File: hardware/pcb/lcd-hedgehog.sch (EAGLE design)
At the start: 40 parts

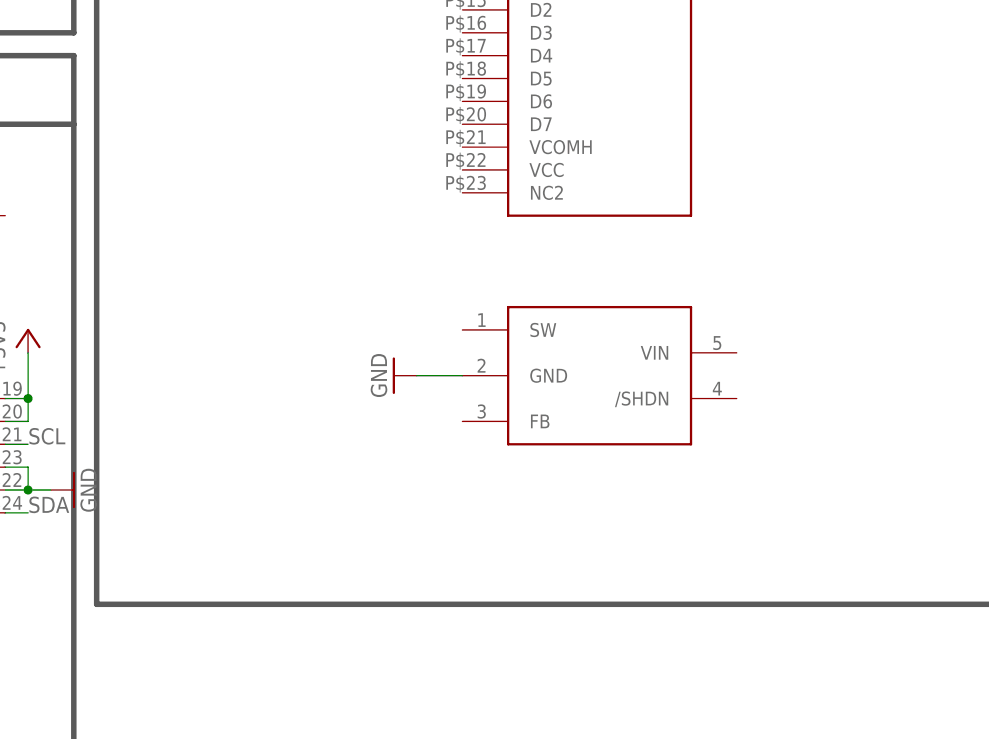
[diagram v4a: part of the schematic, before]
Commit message: added 12V power circuit2
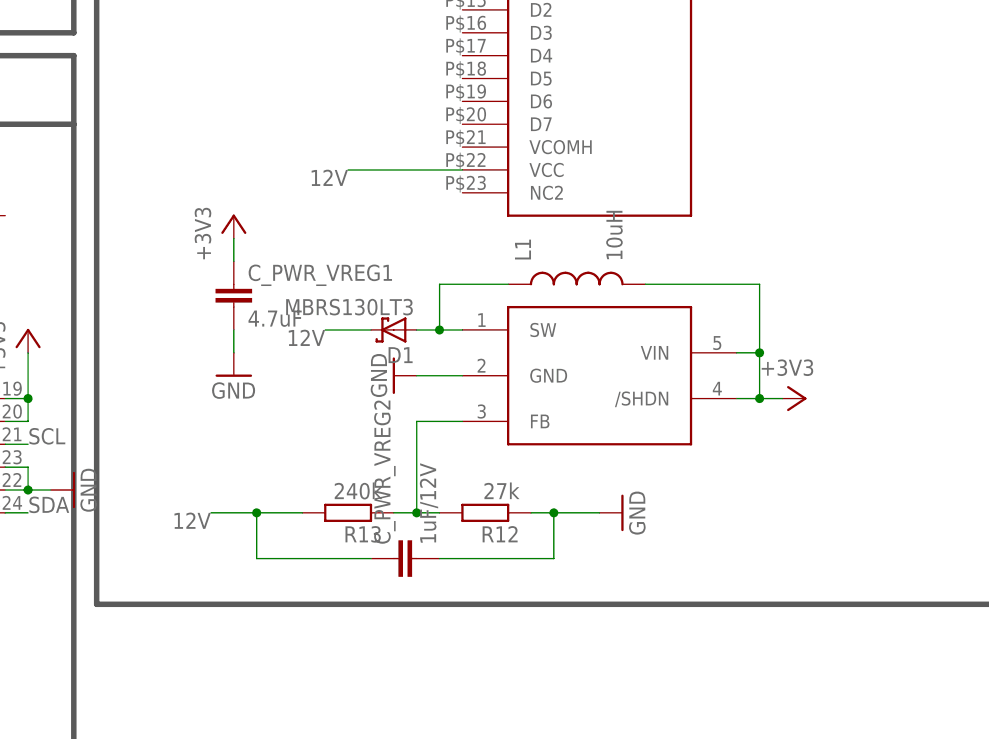
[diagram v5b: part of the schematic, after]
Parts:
- added C_PWR_VREG1: 4.7uF, rcl:C-EUC0603K
- added C_PWR_VREG2: 1uF/12V, rcl:C-EUC0603K
- added D1: MBRS130LT3, diode:MBRS130LT3
- added L1: 10uH, jnode:SPARKFUN_INDUCTOR0603
- added R12: 27k, rcl:R-EU_R0603
- added R13: 240k, rcl:R-EU_R0603
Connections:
- new net 12V: C_PWR_VREG2.1, D1.C, R13.2, U$4.VCC
- new net N$15: R12.2, R13.1, U$5.FB
- new net N$16: D1.A, L1.1, U$5.SW
- net +3V3: now also C_PWR_VREG1.1, L1.2, U$5./SHDN, U$5.VIN
- net GND: now also C_PWR_VREG1.2, C_PWR_VREG2.2, R12.1
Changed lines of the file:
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@@
 <part name="GND32" library="supply1" deviceset="GND" device=""/>
 <part name="C66" library="rcl" deviceset="C-EU" device="C0805K" value="10uF"/>
+<part name="C_PWR_VREG1" library="rcl" deviceset="C-EU" device="C0603K" value="4.7uF"/>
+<part name="R12" library="rcl" deviceset="R-EU_" device="R0603" value="27k"/>
+<part name="R13" library="rcl" deviceset="R-EU_" device="R0603" value="240k"/>
+<part name="GND33" library="supply1" deviceset="GND" device=""/>
+<part name="C_PWR_VREG2" library="rcl" deviceset="C-EU" device="C0603K" value="1uF/12V"/>
+<part name="GND34" library="supply1" deviceset="GND" device=""/>
+<part name="+3V19" library="supply1" deviceset="+3V3" device=""/>
+<part name="+3V20" library="supply1" deviceset="+3V3" device=""/>
+<part name="L1" library="jnode" deviceset="SPARKFUN_INDUCTOR" device="0603" value="10uH"/>
+<part name="D1" library="diode" deviceset="MBRS130LT3" device=""/>
 </parts>
 <sheets>
@@
 <instance part="GND32" gate="1" x="160.02" y="-35.56" rot="R90"/>
 <instance part="C66" gate="G$1" x="149.86" y="-35.56" rot="R90"/>
+<instance part="C_PWR_VREG1" gate="G$1" x="193.04" y="38.1"/>
+<instance part="R12" gate="G$1" x="220.98" y="12.7" rot="R180"/>
+<instance part="R13" gate="G$1" x="205.74" y="12.7" rot="R180"/>
+<instance part="GND33" gate="1" x="236.22" y="12.7" rot="R90"/>
+<instance part="C_PWR_VREG2" gate="G$1" x="210.82" y="7.62" rot="R90"/>
+<instance part="GND34" gate="1" x="193.04" y="27.94"/>
+<instance part="+3V19" gate="G$1" x="193.04" y="45.72"/>
+<instance part="+3V20" gate="G$1" x="256.54" y="25.4" rot="R270"/>
+<instance part="L1" gate="G$1" x="231.14" y="38.1" rot="R90"/>
+<instance part="D1" gate="G$1" x="210.82" y="33.02" rot="R180"/>
 </instances>
 <busses>
@@
 <wire x1="154.94" y1="-35.56" x2="157.48" y2="-35.56" width="0.1524" layer="91"/>
 </segment>
+<segment>
+<pinref part="R12" gate="G$1" pin="1"/>
+<pinref part="GND33" gate="1" pin="GND"/>
+<wire x1="226.06" y1="12.7" x2="228.6" y2="12.7" width="0.1524" layer="91"/>
+<pinref part="C_PWR_VREG2" gate="G$1" pin="2"/>
+<wire x1="228.6" y1="12.7" x2="233.68" y2="12.7" width="0.1524" layer="91"/>
+<wire x1="215.9" y1="7.62" x2="228.6" y2="7.62" width="0.1524" layer="91"/>
+<wire x1="228.6" y1="7.62" x2="228.6" y2="12.7" width="0.1524" layer="91"/>
+<junction x="228.6" y="12.7"/>
+</segment>
+<segment>
+<pinref part="GND34" gate="1" pin="GND"/>
+<pinref part="C_PWR_VREG1" gate="G$1" pin="2"/>
+<wire x1="193.04" y1="33.02" x2="193.04" y2="30.48" width="0.1524" layer="91"/>
+</segment>
 </net>
 <net name="D+" class="0">
@@
 <junction x="144.78" y="-35.56"/>
 <junction x="144.78" y="-15.24"/>
+</segment>
+<segment>
+<pinref part="+3V19" gate="G$1" pin="+3V3"/>
+<pinref part="C_PWR_VREG1" gate="G$1" pin="1"/>
+<wire x1="193.04" y1="40.64" x2="193.04" y2="43.18" width="0.1524" layer="91"/>
+</segment>
+<segment>
+<pinref part="U$5" gate="G$1" pin="/SHDN"/>
+<pinref part="+3V20" gate="G$1" pin="+3V3"/>
+<wire x1="254" y1="25.4" x2="251.46" y2="25.4" width="0.1524" layer="91"/>
+<pinref part="U$5" gate="G$1" pin="VIN"/>
+<wire x1="251.46" y1="25.4" x2="248.92" y2="25.4" width="0.1524" layer="91"/>
+<wire x1="248.92" y1="30.48" x2="251.46" y2="30.48" width="0.1524" layer="91"/>
+<wire x1="251.46" y1="30.48" x2="251.46" y2="25.4" width="0.1524" layer="91"/>
+<junction x="251.46" y="25.4"/>
+<pinref part="L1" gate="G$1" pin="2"/>
+<wire x1="238.76" y1="38.1" x2="251.46" y2="38.1" width="0.1524" layer="91"/>
+<wire x1="251.46" y1="38.1" x2="251.46" y2="30.48" width="0.1524" layer="91"/>
+<junction x="251.46" y="30.48"/>
 </segment>
 </net>
@@
 </segment>
 </net>
+<net name="N$15" class="0">
+<segment>
+<pinref part="R12" gate="G$1" pin="2"/>
+<pinref part="R13" gate="G$1" pin="1"/>
+<wire x1="215.9" y1="12.7" x2="213.36" y2="12.7" width="0.1524" layer="91"/>
+<pinref part="U$5" gate="G$1" pin="FB"/>
+<wire x1="213.36" y1="12.7" x2="210.82" y2="12.7" width="0.1524" layer="91"/>
+<wire x1="218.44" y1="22.86" x2="213.36" y2="22.86" width="0.1524" layer="91"/>
+<wire x1="213.36" y1="22.86" x2="213.36" y2="12.7" width="0.1524" layer="91"/>
+<junction x="213.36" y="12.7"/>
+</segment>
+</net>
+<net name="12V" class="0">
+<segment>
+<pinref part="R13" gate="G$1" pin="2"/>
+<wire x1="200.66" y1="12.7" x2="195.58" y2="12.7" width="0.1524" layer="91"/>
+<label x="190.5" y="12.7" size="1.778" layer="95" rot="R180"/>
+<wire x1="195.58" y1="12.7" x2="190.5" y2="12.7" width="0.1524" layer="91"/>
+<wire x1="195.58" y1="12.7" x2="195.58" y2="7.62" width="0.1524" layer="91"/>
+<pinref part="C_PWR_VREG2" gate="G$1" pin="1"/>
+<wire x1="195.58" y1="7.62" x2="208.28" y2="7.62" width="0.1524" layer="91"/>
+<junction x="195.58" y="12.7"/>
+</segment>
+<segment>
+<pinref part="D1" gate="G$1" pin="C"/>
+<wire x1="208.28" y1="33.02" x2="203.2" y2="33.02" width="0.1524" layer="91"/>
+<label x="203.2" y="33.02" size="1.778" layer="95" rot="R180"/>
+</segment>
+<segment>
+<pinref part="U$4" gate="G$1" pin="VCC"/>
+<wire x1="218.44" y1="50.8" x2="205.74" y2="50.8" width="0.1524" layer="91"/>
+<label x="205.74" y="50.8" size="1.778" layer="95" rot="R180"/>
+</segment>
+</net>
+<net name="N$16" class="0">
+<segment>
+<pinref part="U$5" gate="G$1" pin="SW"/>
+<pinref part="D1" gate="G$1" pin="A"/>
+<wire x1="218.44" y1="33.02" x2="215.9" y2="33.02" width="0.1524" layer="91"/>
+<wire x1="215.9" y1="33.02" x2="213.36" y2="33.02" width="0.1524" layer="91"/>
+<wire x1="215.9" y1="33.02" x2="215.9" y2="38.1" width="0.1524" layer="91"/>
+<pinref part="L1" gate="G$1" pin="1"/>
+<wire x1="215.9" y1="38.1" x2="223.52" y2="38.1" width="0.1524" layer="91"/>
+<junction x="215.9" y="33.02"/>
+</segment>
+</net>

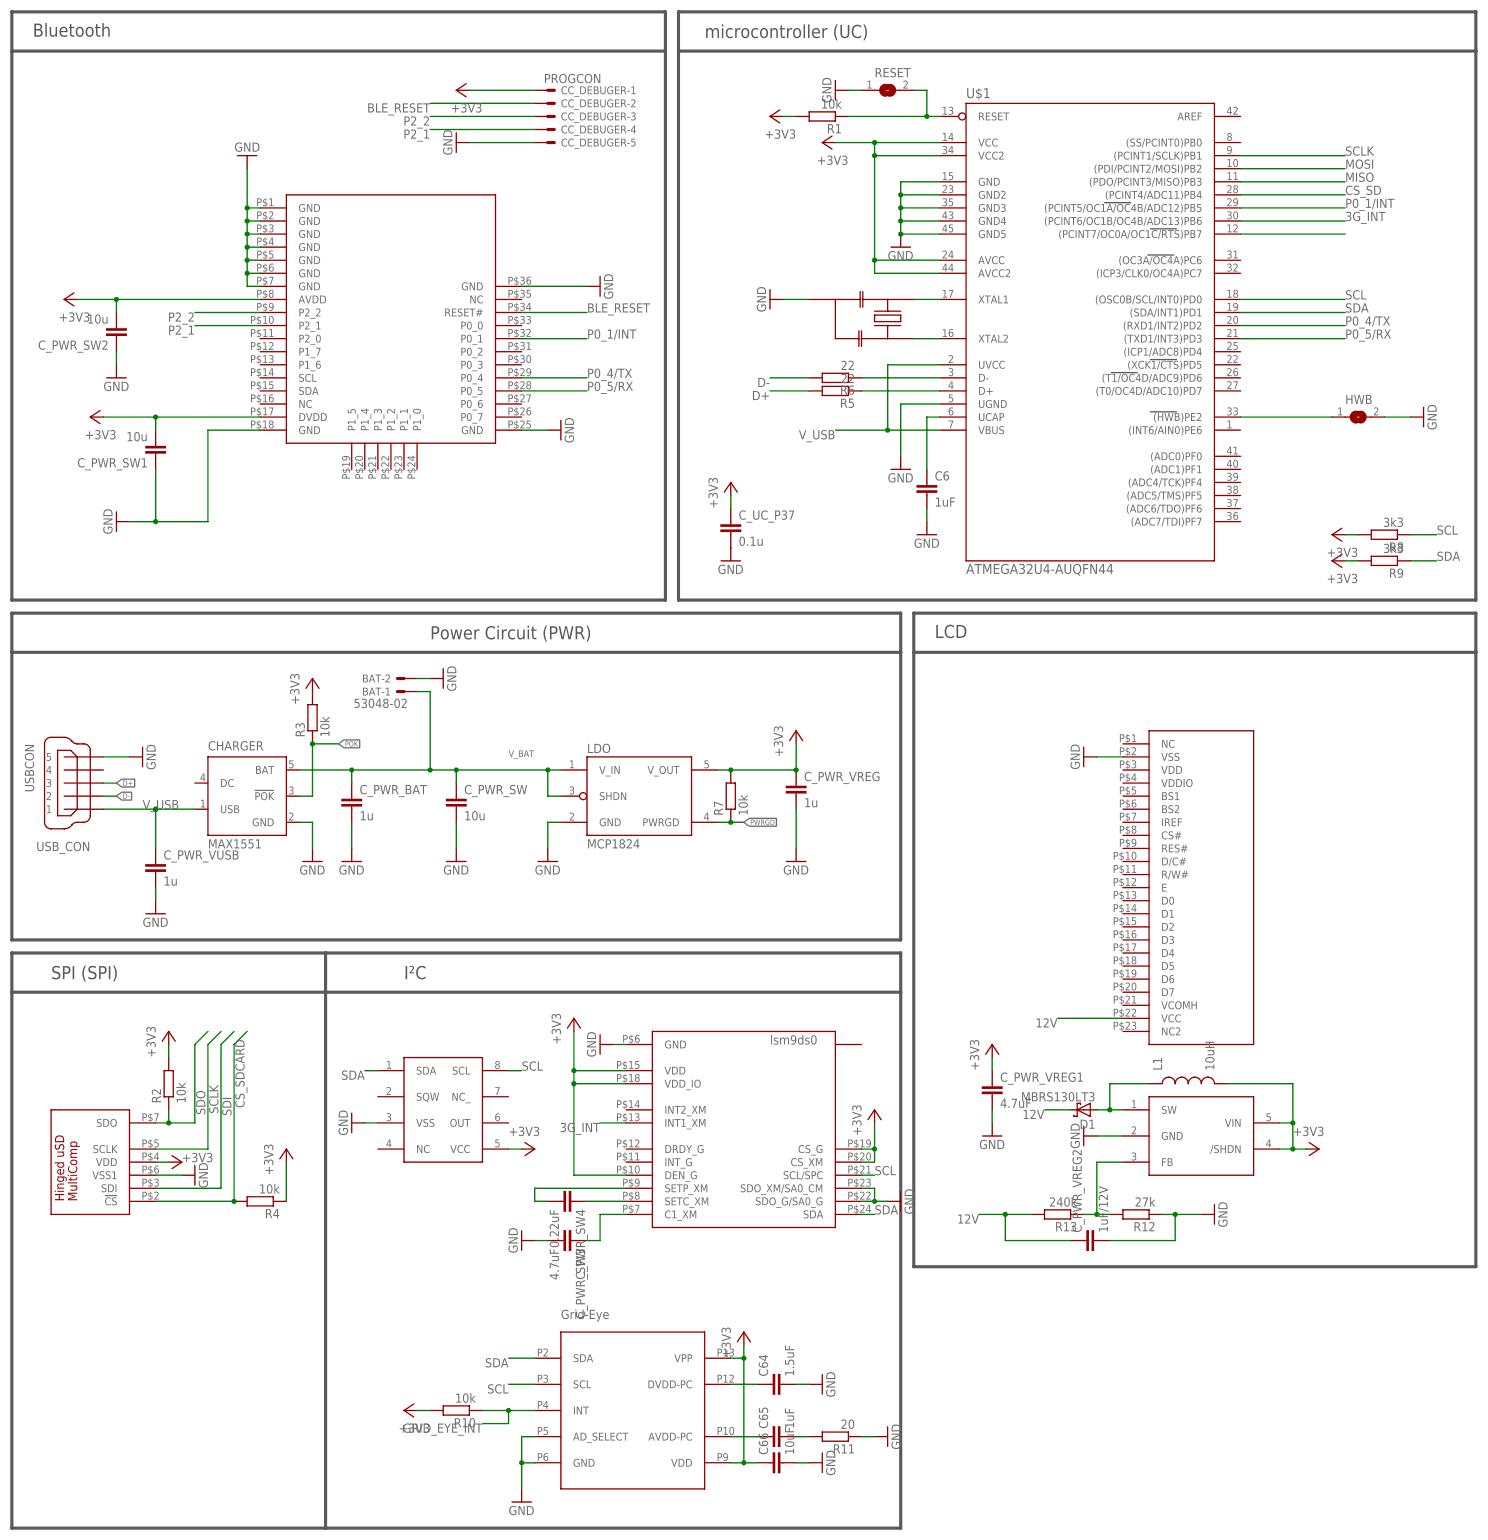
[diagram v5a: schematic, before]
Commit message: connected Display & first placement
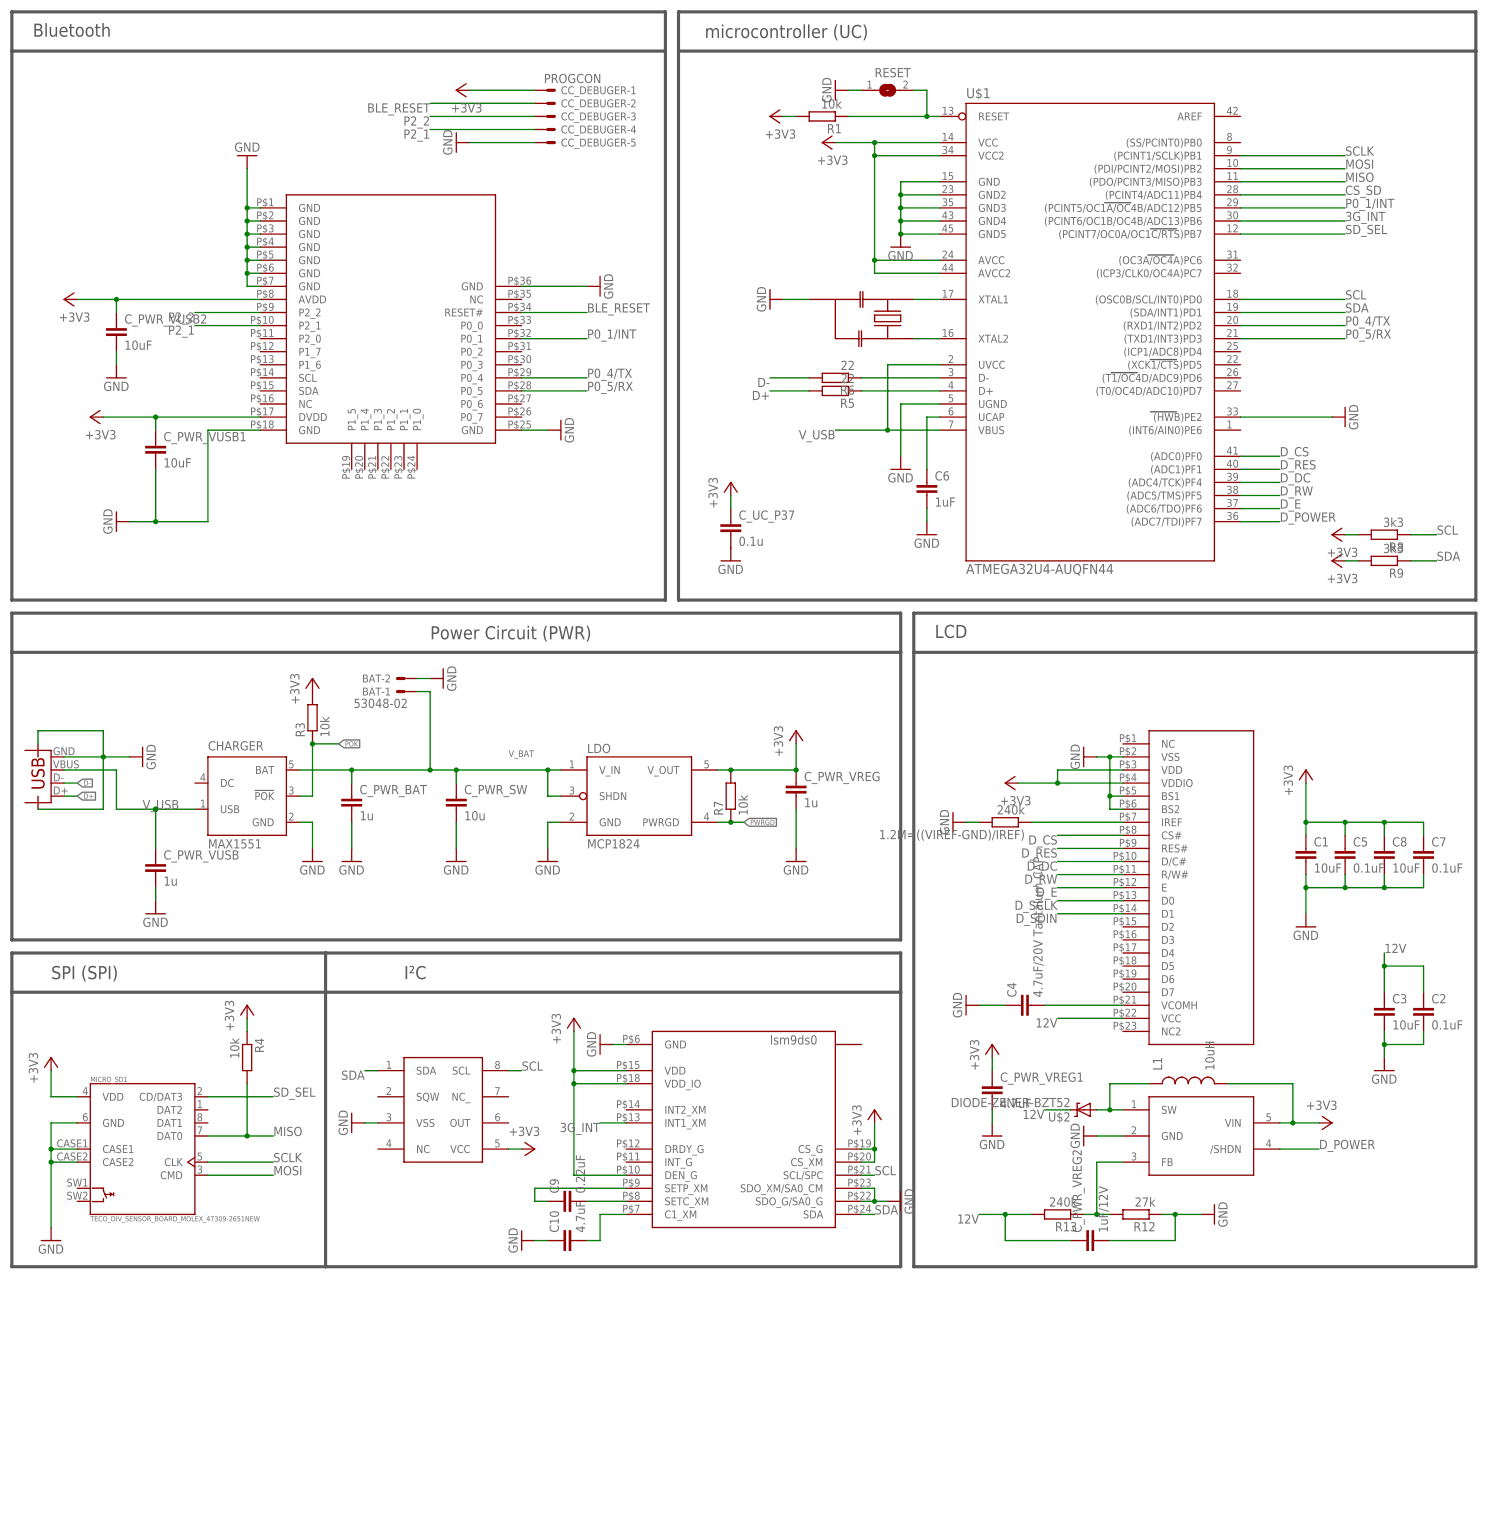
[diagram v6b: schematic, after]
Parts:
- removed C64: 1.5uF, rcl:C-EUC0805K
- removed C65: 1uF, rcl:C-EUC0805K
- removed C66: 10uF, rcl:C-EUC0805K
- removed C_PWR_SW1, C_PWR_SW2: 10u, rcl:C-EUC0805K
- removed C_PWR_SW3: 4.7uF, rcl:C-EUC0805K
- removed C_PWR_SW4: 0.22uF, rcl:C-EUC0805K
- removed D1: MBRS130LT3, diode:MBRS130LT3
- removed HWB: (no value), jumper:SJ
- removed R10, R2: 10k, rcl:R-EU_R0603
- removed R11: 20, rcl:R-EU_R0603
- removed SDCARD_CON: MICROSD_CONN, HedgehogLib:MICROSD_CONN
- removed USB_CON: USBCON, HedgehogLib:USBCON
- added 1.2M=((VIREF-GND)/IREF): 240k, rcl:R-EU_R0603
- added C1, C3, C8, C_PWR_VUSB1, C_PWR_VUSB2: 10uF, rcl:C-EUC0603K
- added C10: 4.7uF, rcl:C-EUC0603K
- added C2, C5, C7: 0.1uF, rcl:C-EUC0603K
- added C4: 4.7uF/20V Tantalum CAP, rcl:C-EUC0603K
- added C9: 0.22uF, rcl:C-EUC0603K
- added MICRO_SD1: TECO_DIV_SENSOR_BOARD_MOLEX_47309-2651NEW, jnode_v32:TECO_DIV_SENSOR_BOARD_MOLEX_47309-2651NEW
- added X1: SPARKFUN_USB-MICROB, jnode_v32:SPARKFUN_USB-MICROB
- U$2: value GRID-EYE -> DIODE-ZENER-BZT52; device HedgehogLib:GRID-EYE -> SparkFun-DiscreteSemi:DIODE-ZENER-BZT52
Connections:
- removed net CS_SDCARD: R4.2, SDCARD_CON.!CS
- removed net GRID_EYE_INT: R10.1, U$2.INT
- removed net N$10: U$1.(PCINT7/OC0A/OC1C/RTS)PB7
- removed net N$12: C64.1, U$2.DVDD-PC
- removed net N$13: C65.1, U$2.AVDD-PC
- removed net N$14: C65.2, R11.2
- removed net N$4: HWB.1, U$1.(HWB)PE2
- removed net SDI: SDCARD_CON.SDI
- removed net SDO: R2.1, SDCARD_CON.SDO
- new net D_CS: U$1.(ADC0)PF0, U$4.CS#
- new net D_DC: U$1.(ADC4/TCK)PF4, U$4.D/C#
- new net D_E: U$1.(ADC6/TDO)PF6, U$4.E
- new net D_POWER: U$1.(ADC7/TDI)PF7, U$5./SHDN
- new net D_RES: U$1.(ADC1)PF1, U$4.RES#
- new net D_RW: U$1.(ADC5/TMS)PF5, U$4.R/W#
- new net D_SCLK: U$4.D0
- new net D_SDIN: U$4.D1
- new net N$22: C4.2, U$4.VCOMH
- new net N$23: 1.2M=((VIREF-GND)/IREF).1, U$4.IREF
- new net SD_SEL: MICRO_SD1.CD/DAT3, U$1.(PCINT7/OC0A/OC1C/RTS)PB7
- net +3V3: now also C1.1, C5.1, C7.1, C8.1, C_PWR_VUSB1.1, C_PWR_VUSB2.1, MICRO_SD1.VDD, U$4.VDD, U$4.VDDIO; no longer C66.1, C_PWR_SW1.2, C_PWR_SW2.2, R10.2, R2.2, SDCARD_CON.VDD, U$2.VDD, U$2.VPP, U$5./SHDN
- net 12V: now also C2.1, C3.1, U$2.C; no longer D1.C
- net D+: now also X1.D+; no longer USB_CON.3
- net D-: now also X1.D-; no longer USB_CON.2
- net GND: now also 1.2M=((VIREF-GND)/IREF).2, C1.2, C10.1, C2.2, C3.2, C4.1, C5.2, C7.2, C8.2, C_PWR_VUSB1.2, C_PWR_VUSB2.2, MICRO_SD1.CASE1, MICRO_SD1.CASE2, MICRO_SD1.GND, U$1.(HWB)PE2, U$4.BS1, U$4.BS2, X1.CASE@1, X1.CASE@2, X1.GND; no longer C64.2, C66.2, C_PWR_SW1.1, C_PWR_SW2.1, C_PWR_SW3.2, HWB.2, R11.1, SDCARD_CON.VSS1, U$2.AD_SELECT, U$2.GND, USB_CON.5
- net MISO: now also MICRO_SD1.DAT0, R4.2
- net MOSI: now also MICRO_SD1.CMD
- net N$16: now also U$2.A; no longer D1.A
- net N$7: now also C9.2; no longer C_PWR_SW4.1
- net N$8: now also C9.1; no longer C_PWR_SW4.2
- net N$9: now also C10.2; no longer C_PWR_SW3.1
- net SCL: no longer U$2.SCL
- net SCLK: now also MICRO_SD1.CLK; no longer SDCARD_CON.SCLK
- net SDA: no longer U$2.SDA
- net V_USB: now also X1.VBUS; no longer USB_CON.1
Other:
- moved on the sheet: R4
